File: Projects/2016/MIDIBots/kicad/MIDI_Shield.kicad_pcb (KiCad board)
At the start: 2 copper layers, 86.4 x 77.5 mm, 71 parts, among them IC1 PC900V, K1 SRVO1, K2 SRVO2, K3 SRVO3, P10 A3, P11 A4, P12 AUX_12V, P13 AUX_12V, P14 AUX_5V, P15 AUX_5V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

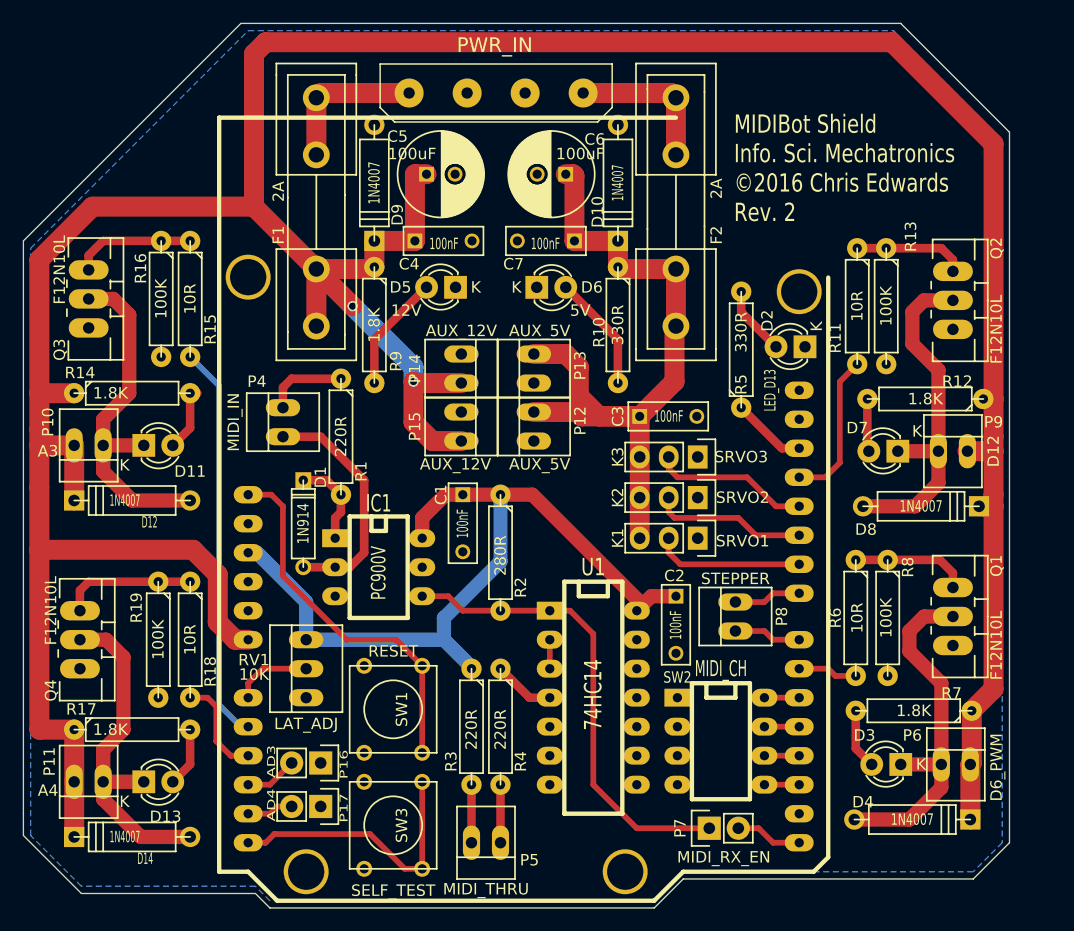
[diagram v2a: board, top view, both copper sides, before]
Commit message: - Somewhat pointless tweaking of the shield outline silkscreening  - Tidied trace under PC900V
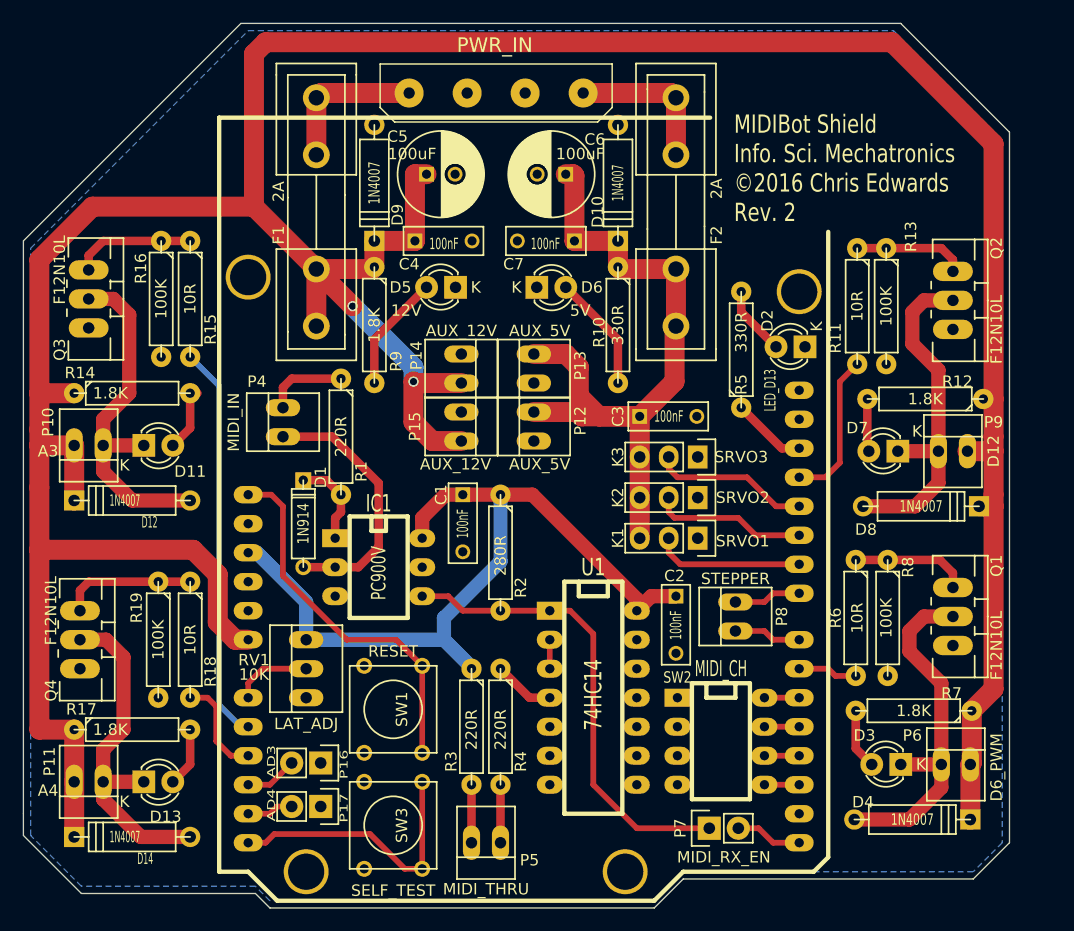
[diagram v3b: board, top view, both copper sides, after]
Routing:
- net Net-(D1-Pad2): track 20.9 -> 23.0 mm
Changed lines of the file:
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@@
     (fp_line (start 66.04 -40.64) (end 66.04 -52.07) (layer F.SilkS) (width 0.381))
     (fp_line (start 66.04 -52.07) (end 64.77 -53.34) (layer F.SilkS) (width 0.381))
-    (fp_line (start 64.77 -53.34) (end 14 -53.34) (layer F.SilkS) (width 0.381))
+    (fp_line (start 64.77 -53.34) (end 10 -53.34) (layer F.SilkS) (width 0.381))
     (fp_line (start 66.04 0) (end 0 0) (layer F.SilkS) (width 0.381))
-    (fp_line (start 0 0) (end 0 -40) (layer F.SilkS) (width 0.381))
+    (fp_line (start 0 0) (end 0 -43) (layer F.SilkS) (width 0.381))
     (fp_line (start 66.04 -40.64) (end 68.58 -38.1) (layer F.SilkS) (width 0.381))
     (fp_line (start 68.58 -38.1) (end 68.58 -5.08) (layer F.SilkS) (width 0.381))
@@
     (at 98.679 103.251 90)
     (attr virtual)
-    (fp_text reference P14 (at 0 -10.414 90) (layer F.SilkS)
+    (fp_text reference P14 (at 1.143 -10.287 90) (layer F.SilkS)
       (effects (font (size 1 1) (thickness 0.15)))
     )
@@
   (segment (start 73.66 130.81) (end 73.66 132.08) (width 0.5) (layer F.Cu) (net 16))
   (segment (start 74.93 129.54) (end 73.66 130.81) (width 0.5) (layer F.Cu) (net 16))
-  (segment (start 121.92 127) (end 119.634 127) (width 0.5) (layer F.Cu) (net 17) (status 400000))
-  (segment (start 118.872 126.238) (end 116.332 126.238) (width 0.5) (layer F.Cu) (net 17) (status 800000))
+  (segment (start 121.92 127) (end 119.634 127) (width 0.5) (layer F.Cu) (net 17))
+  (segment (start 118.872 126.238) (end 116.332 126.238) (width 0.5) (layer F.Cu) (net 17))
   (segment (start 119.634 127) (end 118.872 126.238) (width 0.5) (layer F.Cu) (net 17))
-  (segment (start 121.92 122.936) (end 119.634 122.936) (width 0.5) (layer F.Cu) (net 18) (status 400000))
-  (segment (start 118.872 123.698) (end 116.332 123.698) (width 0.5) (layer F.Cu) (net 18) (status 800000))
+  (segment (start 121.92 122.936) (end 119.634 122.936) (width 0.5) (layer F.Cu) (net 18))
+  (segment (start 118.872 123.698) (end 116.332 123.698) (width 0.5) (layer F.Cu) (net 18))
   (segment (start 119.634 122.936) (end 118.872 123.698) (width 0.5) (layer F.Cu) (net 18))
   (segment (start 121.92 120.396) (end 111.506 120.396) (width 0.5) (layer F.Cu) (net 19))
@@
   (segment (start 81.28 116.332) (end 81.28 118.11) (width 0.75) (layer F.Cu) (net 33))
   (segment (start 81.788 115.824) (end 81.28 116.332) (width 0.75) (layer F.Cu) (net 33))
-  (segment (start 76.708 109.22) (end 80.01 109.22) (width 0.75) (layer F.Cu) (net 34))
-  (segment (start 82.55 120.65) (end 81.28 120.65) (width 0.75) (layer F.Cu) (net 34))
-  (segment (start 83.82 119.38) (end 82.55 120.65) (width 0.75) (layer F.Cu) (net 34))
-  (segment (start 83.82 113.03) (end 83.82 119.38) (width 0.75) (layer F.Cu) (net 34))
-  (segment (start 80.01 109.22) (end 83.82 113.03) (width 0.75) (layer F.Cu) (net 34))
+  (segment (start 76.708 109.22) (end 81.026 109.22) (width 0.75) (layer F.Cu) (net 34))
+  (segment (start 83.312 120.65) (end 81.28 120.65) (width 0.75) (layer F.Cu) (net 34))
+  (segment (start 85.09 118.872) (end 83.312 120.65) (width 0.75) (layer F.Cu) (net 34))
+  (segment (start 85.09 113.284) (end 85.09 118.872) (width 0.75) (layer F.Cu) (net 34))
+  (segment (start 81.026 109.22) (end 85.09 113.284) (width 0.75) (layer F.Cu) (net 34))
   (segment (start 78.486 120.65) (end 81.28 120.65) (width 0.75) (layer F.Cu) (net 34))
   (segment (start 116.84 96.52) (end 116.84 98.298) (width 0.75) (layer F.Cu) (net 35))

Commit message: Repositioned LED on Arduino pin D13 to avoid the SDA and SCL header pins on newer Arduino models.
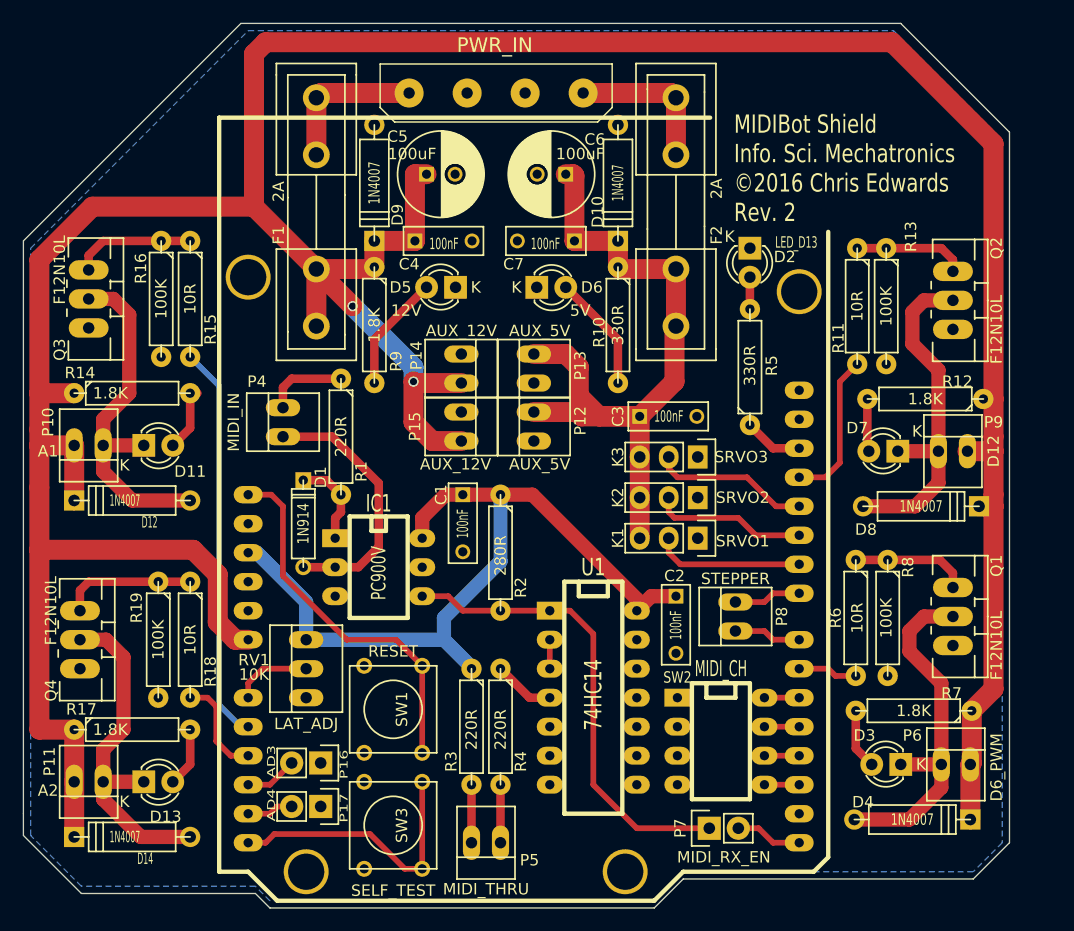
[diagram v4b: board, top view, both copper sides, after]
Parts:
- P10: value A3 -> A1
- P11: value A4 -> A2
- moved D2 9.89 mm to (117.6, 92.7), turned to 270 degrees
- moved R5 1.70 mm to (117.6, 103.1)
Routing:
- net Net-(D2-Pad2): track 6.09 -> 2.79 mm
- net /LED_BUILTIN: track 6.55 -> 5.16 mm
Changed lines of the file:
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@@
-(kicad_pcb (version 4) (host pcbnew 4.0.2+dfsg1-2~bpo8+1-stable)
+(kicad_pcb (version 4) (host pcbnew 4.0.2-stable)
   (general
     (links 151)
     (no_connects 0)
-    (area 49.899999 59.899999 150.100001 160.100001)
+    (area 53.924999 72.974999 140.385001 150.545001)
     (thickness 1.6)
     (drawings 18)
-    (tracks 261)
+    (tracks 260)
     (zones 0)
     (modules 71)
@@
   )
   (module LEDs:LED-3MM (layer F.Cu)
-    (at 122.428 101.346 180)
+    (at 117.602 92.71 270)
     (descr "LED 3mm round vertical")
     (tags "LED  3mm round vertical")
-    (fp_text reference D2 (at 3.302 2.286 270) (layer F.SilkS)
-      (effects (font (size 1 1) (thickness 0.15)))
-    )
-    (fp_text value LED_D13 (at 3.048 -3.81 270) (layer F.SilkS)
+    (fp_text reference D2 (at 0.762 -3.048 360) (layer F.SilkS)
+      (effects (font (size 1 1) (thickness 0.15)))
+    )
+    (fp_text value LED_D13 (at -0.508 -4.064 360) (layer F.SilkS)
       (effects (font (size 1 0.6) (thickness 0.15)))
     )
@@
     (fp_arc (start 1.311 0.034) (end 3.051 0.994) (angle 110) (layer F.SilkS) (width 0.15))
     (fp_arc (start 1.301 0.034) (end 2.335 1.094) (angle 87.5) (layer F.SilkS) (width 0.15))
-    (fp_text user K (at -1.016 1.778 270) (layer F.SilkS)
-      (effects (font (size 1 1) (thickness 0.15)))
-    )
-    (pad 1 thru_hole rect (at 0 0 270) (size 2 2) (drill 1.00076) (layers *.Cu *.Mask F.SilkS)
-      (net 7 GND))
-    (pad 2 thru_hole circle (at 2.54 0 180) (size 2 2) (drill 1.00076) (layers *.Cu *.Mask F.SilkS)
+    (fp_text user K (at -1.016 1.778 360) (layer F.SilkS)
+      (effects (font (size 1 1) (thickness 0.15)))
+    )
+    (pad 1 thru_hole rect (at 0 0) (size 2 2) (drill 1.00076) (layers *.Cu *.Mask F.SilkS)
+      (net 7 GND))
+    (pad 2 thru_hole circle (at 2.54 0 270) (size 2 2) (drill 1.00076) (layers *.Cu *.Mask F.SilkS)
       (net 35 "Net-(D2-Pad2)"))
     (model LEDs.3dshapes/LED-3MM.wrl
@@
       (effects (font (size 1 1) (thickness 0.15)))
     )
-    (fp_text value A3 (at 3.556 -0.508 180) (layer F.SilkS)
+    (fp_text value A1 (at 3.556 -0.508 180) (layer F.SilkS)
       (effects (font (size 1 1) (thickness 0.15)))
     )
@@
       (effects (font (size 1 1) (thickness 0.15)))
     )
-    (fp_text value A4 (at 3.556 -0.762 180) (layer F.SilkS)
+    (fp_text value A2 (at 3.556 -0.762 180) (layer F.SilkS)
       (effects (font (size 1 1) (thickness 0.15)))
     )
@@
   )
   (module Discret:R4-LARGE_PADS (layer F.Cu)
-    (at 116.84 101.6 90)
+    (at 117.602 103.124 90)
     (descr "Resitance 4 pas")
     (tags R)
-    (fp_text reference R5 (at -3.048 0 90) (layer F.SilkS)
-      (effects (font (size 1 1) (thickness 0.15)))
-    )
-    (fp_text value 330R (at 1.524 0 90) (layer F.SilkS)
+    (fp_text reference R5 (at 0.127 1.905 90) (layer F.SilkS)
+      (effects (font (size 1 1) (thickness 0.15)))
+    )
+    (fp_text value 330R (at 0.127 0 90) (layer F.SilkS)
       (effects (font (size 1 1) (thickness 0.15)))
     )
@@
     (descr "Resitance 4 pas")
     (tags R)
-    (fp_text reference R11 (at 2.794 1.905 450) (layer F.SilkS)
+    (fp_text reference R11 (at 2.794 1.651 450) (layer F.SilkS)
       (effects (font (size 1 1) (thickness 0.15)))
     )
@@
   (segment (start 84.53374 94.53626) (end 79.629 94.53626) (width 1.75) (layer F.Cu) (net 25))
   (segment (start 79.629 94.53626) (end 79.629 99.53498) (width 1.75) (layer F.Cu) (net 25))
-  (segment (start 121.92 110.236) (end 120.396 110.236) (width 0.75) (layer F.Cu) (net 26))
-  (segment (start 120.396 110.236) (end 116.84 106.68) (width 0.75) (layer F.Cu) (net 26))
+  (segment (start 121.92 110.236) (end 119.634 110.236) (width 0.75) (layer F.Cu) (net 26))
+  (segment (start 119.634 110.236) (end 117.602 108.204) (width 0.75) (layer F.Cu) (net 26))
   (segment (start 121.92 144.78) (end 119.634 144.78) (width 0.5) (layer F.Cu) (net 27))
   (segment (start 118.364 143.51) (end 116.586 143.51) (width 0.5) (layer F.Cu) (net 27))
@@
   (segment (start 81.026 109.22) (end 85.09 113.284) (width 0.75) (layer F.Cu) (net 34))
   (segment (start 78.486 120.65) (end 81.28 120.65) (width 0.75) (layer F.Cu) (net 34))
-  (segment (start 116.84 96.52) (end 116.84 98.298) (width 0.75) (layer F.Cu) (net 35))
-  (segment (start 116.84 98.298) (end 119.888 101.346) (width 0.75) (layer F.Cu) (net 35))
+  (segment (start 117.602 98.044) (end 117.602 95.25) (width 0.75) (layer F.Cu) (net 35))
   (segment (start 84.709 104.521) (end 84.709 100.711) (width 0.75) (layer F.Cu) (net 36))
   (segment (start 84.709 100.711) (end 89.281 96.139) (width 0.75) (layer F.Cu) (net 36))

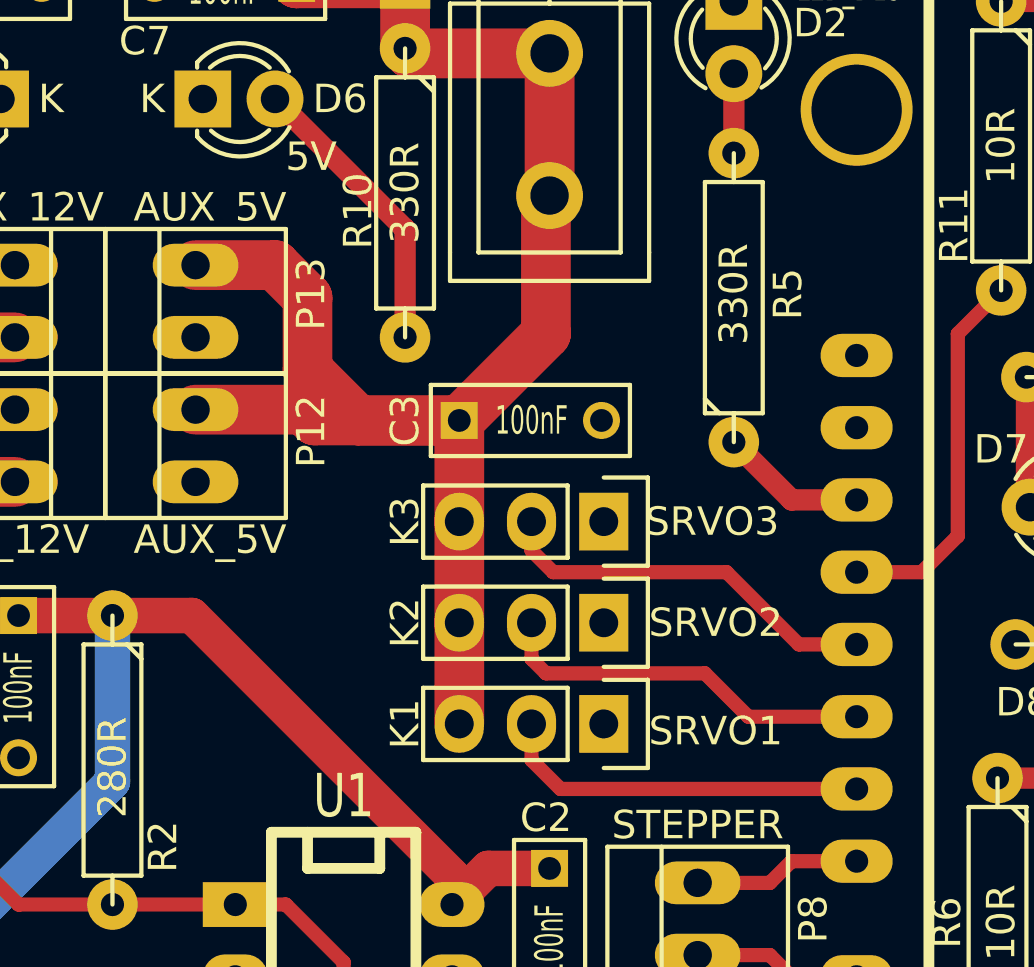
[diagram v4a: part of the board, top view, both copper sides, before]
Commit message: Fixed servo pinouts
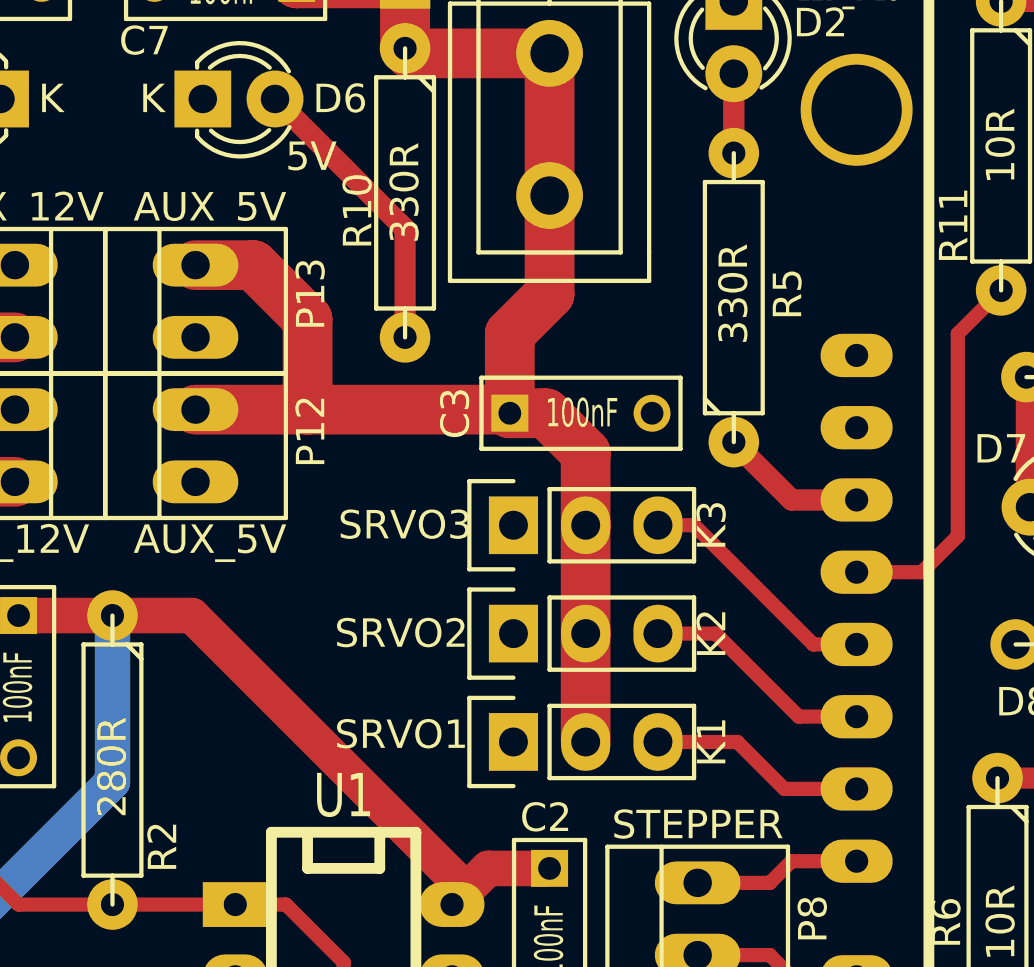
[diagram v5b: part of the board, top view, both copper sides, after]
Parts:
- moved K1 3.24 mm to (109.9, 118.7), turned to 90 degrees
- moved K2 3.20 mm to (109.9, 114.9), turned to 90 degrees
- moved K3 3.18 mm to (109.9, 111.1), turned to 90 degrees
- moved C3 1.80 mm to (109.7, 107.2)
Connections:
- K1 pad 2: /SERVO_1 -> +5V
- K1 pad 3: +5V -> /SERVO_1
- K2 pad 2: /SERVO_2 -> +5V
- K2 pad 3: +5V -> /SERVO_2
- K3 pad 2: /SERVO_3 -> +5V
- K3 pad 3: +5V -> /SERVO_3
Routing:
- net /SERVO_1: track 13.1 -> 7.67 mm
- net /SERVO_2: track 13.5 -> 8.19 mm
- net /SERVO_3: track 13.8 -> 8.72 mm
- net +5V: track 65.1 -> 63.6 mm
